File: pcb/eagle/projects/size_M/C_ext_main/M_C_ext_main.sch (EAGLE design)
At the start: 18 parts

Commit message: PCB M.1
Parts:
- removed H.C1, H.C5, H.C6, H.C7, H.C8, H.C9: 100n, rcl:C-EUC0603
- removed H.C3: 1u, rcl:C-EUC0603
- removed H.C4: 10u (22u), rcl:C-EUC0805
- removed H.J1, H.J2: (no value), pinhead2:PINHD-1X6
- removed H.R1, H.R2: 100k, rcl:R-EU_R0603
- removed H.R3: 10k, rcl:R-EU_R0603
- removed H.U1: WT2003S, WT2003S:WT2003S
- removed H.U2: TPA6211, hugo:TPA6211
- removed H.USB: USB-C, hugo:USB-C
- removed JP2: (no value), pinhead2:PINHD-1X4
- added C.C1, C.C2, C.C4: 100n, rcl:C-EUC0603
- added C.C3: 22u, rcl:C-EUC0805
- added C.C5: 10u, rcl:C-EUC0603
- added C.J2: (no value), pinhead2:PINHD-1X6
- added C.R1, C.R2: 2k2, rcl:R-EU_R0603
- added C.R3, C.R4: 0, rcl:R-EU_R0603
- added C.U1: TTGO-MICRO-32, hugo:TTGO-MICRO-32
- added U$1: USB-C, hugo:USB-C
- added U1: CP2104-F03-GM, CP2104:CP2104-F03-GM
- JP1: device pinhead2:PINHD-1X3 -> pinhead2:PINHD-1X4
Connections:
- removed net N$10: H.U1.DM, H.USB.D1_N, H.USB.D2_N
- removed net N$11: H.C3.1, H.U1.VDDLDO, H.USB.VBUS1, H.USB.VBUS2
- removed net N$12: H.C6.1, H.C8.1, H.U1.VOUTR
- removed net N$13: H.C7.1, H.C9.1, H.U1.VOUTL
- removed net N$14: H.R1.2, H.R2.2, H.U2.IN+
- removed net N$15: H.C5.2, H.U2.BYPASS, H.U2.IN-
- removed net N$16: H.U1.SDCLK, JP1.1
- removed net N$17: H.C6.2, H.R1.1
- removed net N$18: H.C7.2, H.R2.1
- removed net N$19: H.U1.SDDAT, JP1.3
- removed net N$3: H.J1.5, H.U2.VO-
- removed net N$4: H.J2.3, H.U1.RX
- removed net N$5: H.J2.4, H.U1.TX
- removed net N$6: H.J1.6, H.U2.VO+
- removed net N$7: H.J1.3, H.R3.1, H.U2.SHTDWN
- removed net N$8: H.U1.SDCMD, JP1.2
- removed net N$9: H.U1.DP, H.USB.D1_P, H.USB.D2_P
- new net PROG: C.R4.1, C.R4.2, C.U1.IO0, U1.!DTR
- new net RESET: C.R3.1, C.R3.2, C.U1.EN, U1.!RTS
- new net RX: C.U1.TXD0, U1.RXD
- new net SCL: C.J2.1, C.R1.1, C.U1.IO22
- new net SDA: C.J2.2, C.R2.1, C.U1.IO21
- new net TX: C.U1.RXD0, U1.TXD
- new net VUSB: C.C4.2, C.C5.2, JP1.1, U$1.VBUS1, U$1.VBUS2, U1.REGIN, U1.VBUS
- net GND: now also C.C1.2, C.C2.2, C.C3.2, C.C4.1, C.C5.1, C.J2.6, C.U1.GND, C.U1.GND2, C.U1.GND3, JP1.4, U$1.GND1, U$1.GND2, U1.GND; no longer H.C1.2, H.C3.2, H.C4.1, H.C5.1, H.J1.4, H.J2.6, H.U1.AVSS, H.U1.DVSS, H.U2.GND, H.USB.GND1, H.USB.GND2, JP2.4
- net N$1: now also U$1.D1_N, U1.DN; no longer H.C8.2, H.J1.2
- net N$2: now also U$1.D1_P, U1.DP; no longer H.C9.2, H.J1.1
- net VCC: now also C.C1.1, C.C2.1, C.C3.1, C.R1.2, C.R2.2, C.U1.3V3, JP1.3, U1.VDD; no longer H.C1.1, H.C4.2, H.R3.2, H.U1.VDDIO, H.U2.VDD, JP2.3

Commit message: updated PCBS after the version 1 delivery
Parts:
- removed C.C4: 100n, rcl:C-EUC0603
- added C.R5: 5K1, rcl:R-EU_R0603
- added C.R6: 5k1, rcl:R-EU_R0603
- C.C5: value 10u -> 1u
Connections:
- new net N$3: C.R6.2, U$1.CC1
- new net N$4: C.R5.2, U$1.CC2
- net GND: now also C.R5.1, C.R6.1; no longer C.C4.1
- net N$1: now also U$1.D2_N
- net N$2: now also U$1.D2_P
- net VCC: now also U1.VIO
- net VUSB: no longer C.C4.2
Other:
- moved on the sheet: U$1

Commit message: updated PCBs for version 2
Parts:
- added C.F1, C.F2: (no value), rcl:R-EU_R0805
- added PROGRAMMING: TPB1,27, testpad:TPB1,27
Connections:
- new net N$5: C.F2.2, JP1.3
- new net N$6: C.F1.2, JP1.1
- new net N$7: PROGRAMMING.TP, U1.!RST!
- net VCC: now also C.F2.1; no longer JP1.3
- net VUSB: now also C.F1.1; no longer JP1.1
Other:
- moved on the sheet: C.C2, C.C5, C.R3, C.R4, C.R5, C.R6, JP1, U$1, U1

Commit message: closed PCB version M.2
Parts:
- renumbered PROGRAMMING to PROG
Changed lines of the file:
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@@
 <part name="C.F2" library="rcl" library_urn="urn:adsk.eagle:library:334" deviceset="R-EU_" device="R0805" package3d_urn="urn:adsk.eagle:package:23553/2"/>
 <part name="C.F1" library="rcl" library_urn="urn:adsk.eagle:library:334" deviceset="R-EU_" device="R0805" package3d_urn="urn:adsk.eagle:package:23553/2"/>
-<part name="PROGRAMMING" library="testpad" library_urn="urn:adsk.eagle:library:385" deviceset="TP" device="B1,27" package3d_urn="urn:adsk.eagle:package:27944/2"/>
+<part name="PROG" library="testpad" library_urn="urn:adsk.eagle:library:385" deviceset="TP" device="B1,27" package3d_urn="urn:adsk.eagle:package:27944/2"/>
 </parts>
 <sheets>
@@
 <attribute name="VALUE" x="168.91" y="65.659" size="1.778" layer="96"/>
 </instance>
-<instance part="PROGRAMMING" gate="G$1" x="119.38" y="157.48" smashed="yes">
+<instance part="PROG" gate="G$1" x="119.38" y="157.48" smashed="yes">
 <attribute name="NAME" x="123.19" y="146.05" size="1.778" layer="95" rot="R90"/>
 <attribute name="TP_SIGNAL_NAME" x="120.65" y="156.21" size="1.778" layer="97"/>
@@
 <pinref part="U1" gate="IC" pin="!RST!"/>
 <wire x1="119.38" y1="154.94" x2="116.84" y2="154.94" width="0.1524" layer="91"/>
-<pinref part="PROGRAMMING" gate="G$1" pin="TP"/>
-</segment>
-</net>
+<pinref part="PROG" gate="G$1" pin="TP"/>
+</segment>
+</net>

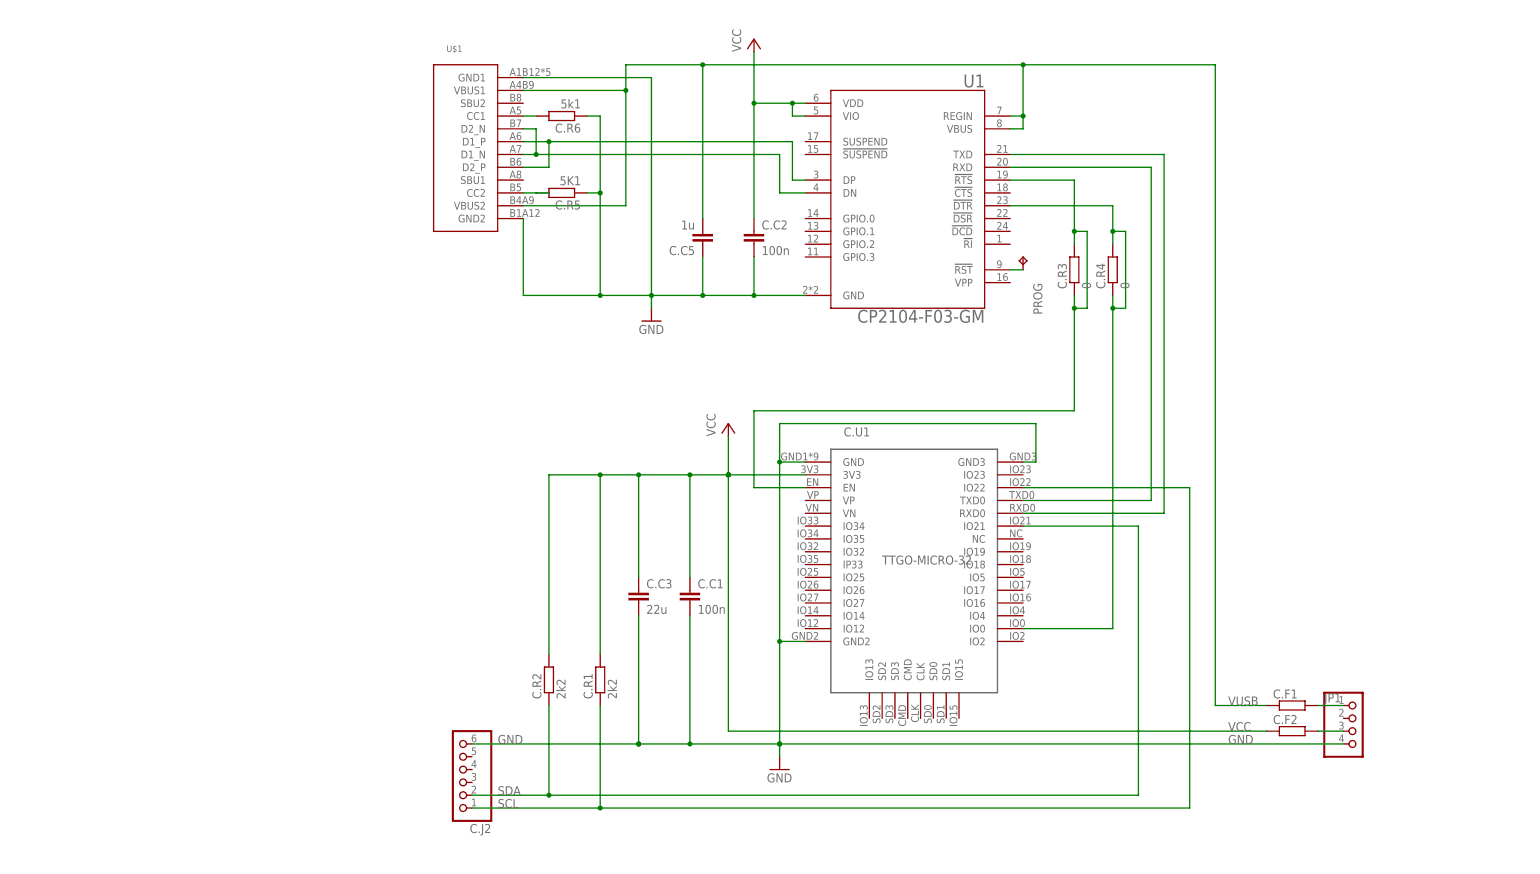
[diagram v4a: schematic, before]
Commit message: updated main board - added 5 to 3.3V regulator becaues one in CP is too weak updated power board - added shotky diode to FET to be sure it works as expected
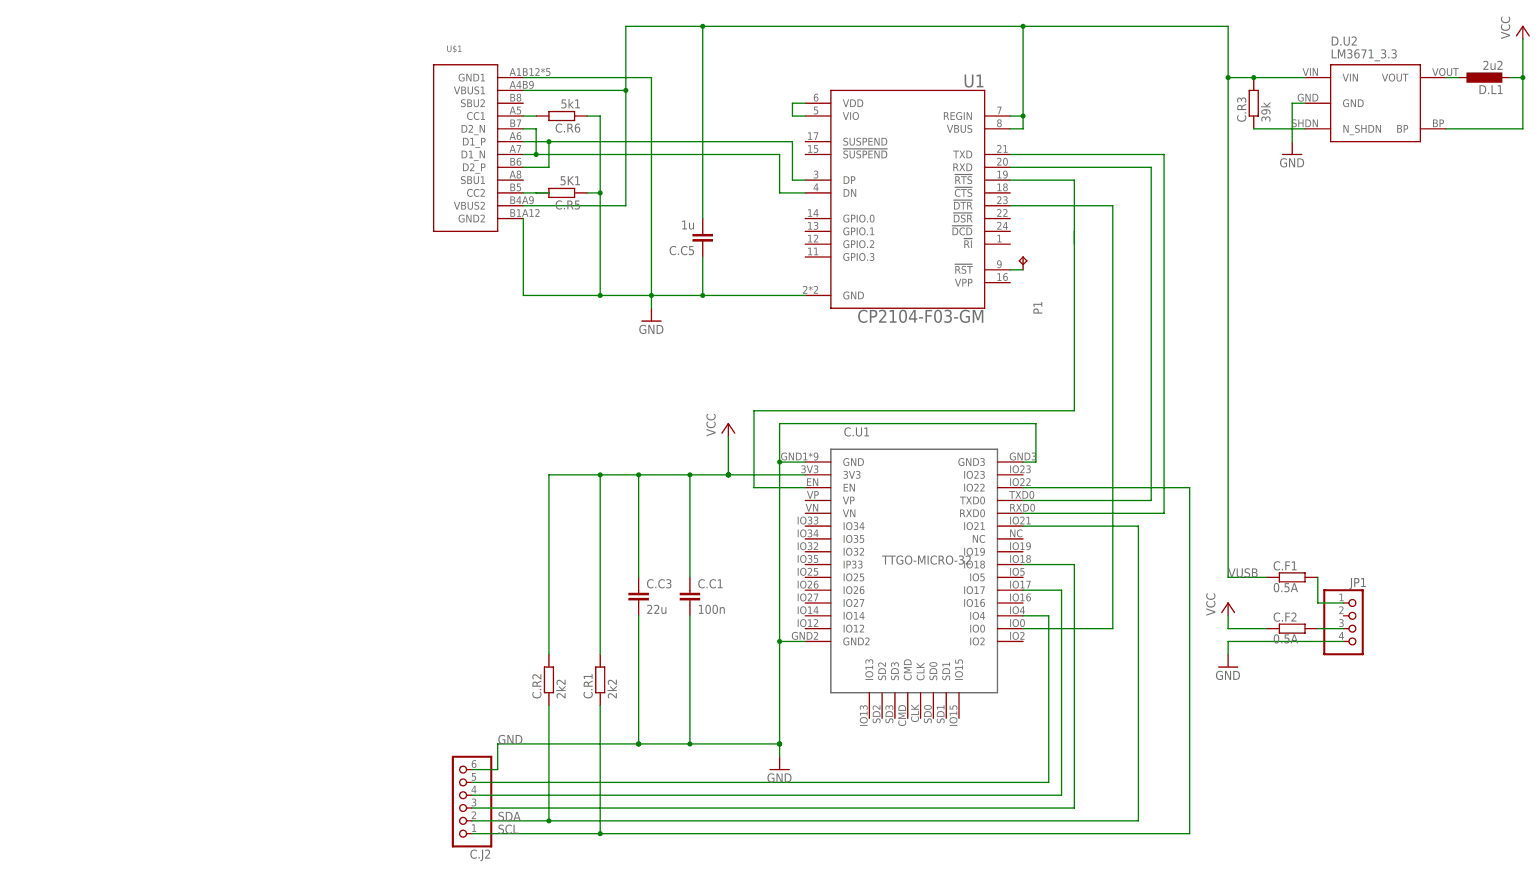
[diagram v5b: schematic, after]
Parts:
- removed C.C2: 100n, rcl:C-EUC0603
- removed C.R4: 0, rcl:R-EU_R0603
- added D.L1: 2u2, rcl:L-EUL3230M
- added D.U2: LM3671_3.3, !stavebnice03:STABILISER_APE8865
- C.F1, C.F2: value (none) -> 0.5A
- C.R3: value 0 -> 39k
- renumbered PROG to P1
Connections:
- new net N$10: D.L1.1, D.U2.VOUT
- new net N$11: C.R3.1, D.U2.N_SHDN
- new net N$12: C.J2.5, C.U1.IO4
- new net N$13: C.J2.4, C.U1.IO17
- new net N$14: C.J2.3, C.U1.IO18
- new net N$8: U1.VDD, U1.VIO
- net GND: now also D.U2.GND; no longer C.C2.2
- net PROG: no longer C.R4.1, C.R4.2
- net RESET: no longer C.R3.1, C.R3.2
- net VCC: now also D.L1.2, D.U2.BP; no longer C.C2.1, U1.VDD, U1.VIO
- net VUSB: now also C.R3.2, D.U2.VIN
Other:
- moved on the sheet: C.F1, C.F2, C.J2, C.R3, JP1

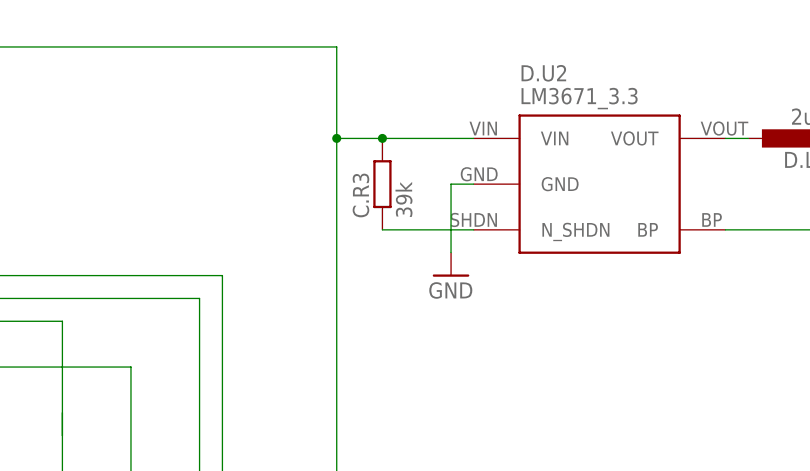
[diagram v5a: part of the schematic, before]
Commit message: main and switch pcbs adjusted
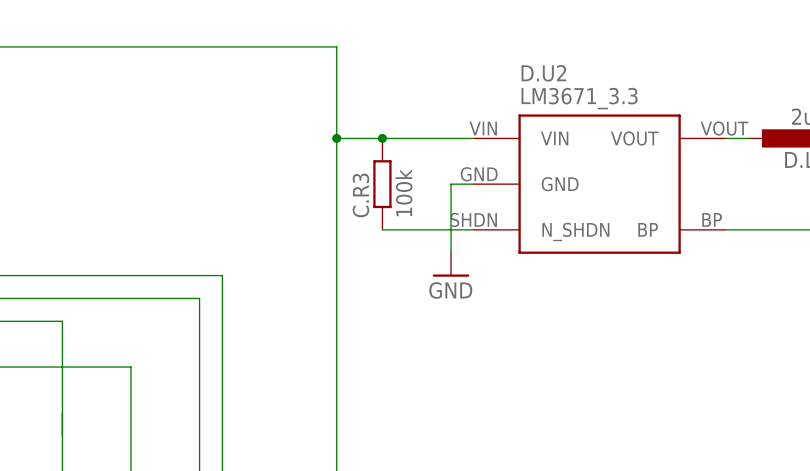
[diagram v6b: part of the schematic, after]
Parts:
- C.R3: value 39k -> 100k
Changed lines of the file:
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@@
 <part name="D.U2" library="!stavebnice03" deviceset="STABILISER_APE8865" device="" value="LM3671_3.3"/>
 <part name="D.L1" library="rcl" library_urn="urn:adsk.eagle:library:334" deviceset="L-EU" device="L3230M" package3d_urn="urn:adsk.eagle:package:23481/3" value="2u2"/>
-<part name="C.R3" library="rcl" library_urn="urn:adsk.eagle:library:334" deviceset="R-EU_" device="R0603" package3d_urn="urn:adsk.eagle:package:23555/3" value="39k"/>
+<part name="C.R3" library="rcl" library_urn="urn:adsk.eagle:library:334" deviceset="R-EU_" device="R0603" package3d_urn="urn:adsk.eagle:package:23555/3" value="100k"/>
 <part name="GND3" library="supply1" library_urn="urn:adsk.eagle:library:371" deviceset="GND" device=""/>
 <part name="P+3" library="supply1" library_urn="urn:adsk.eagle:library:371" deviceset="VCC" device=""/>

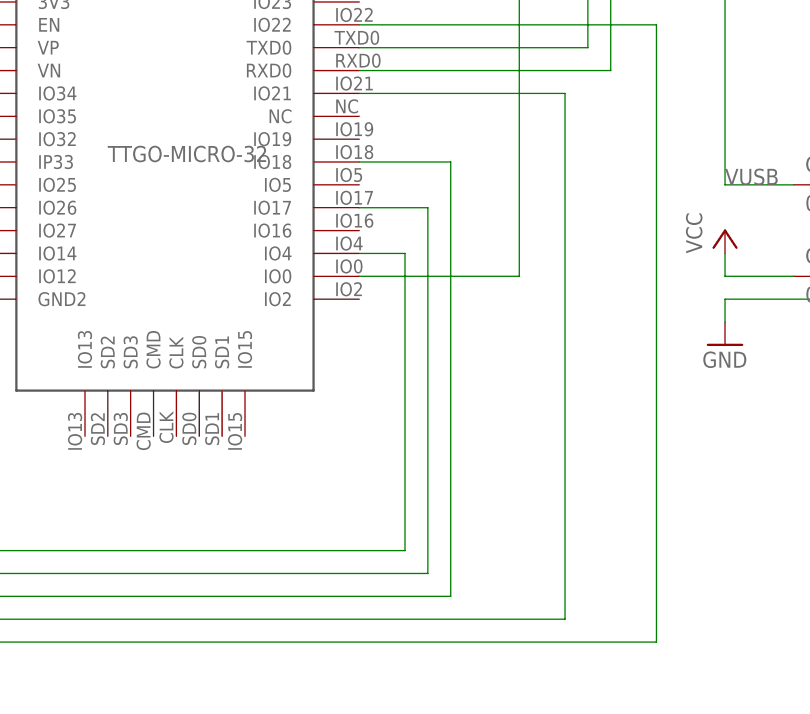
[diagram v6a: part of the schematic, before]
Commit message: changed one data bit to be compatible with T-micro32+
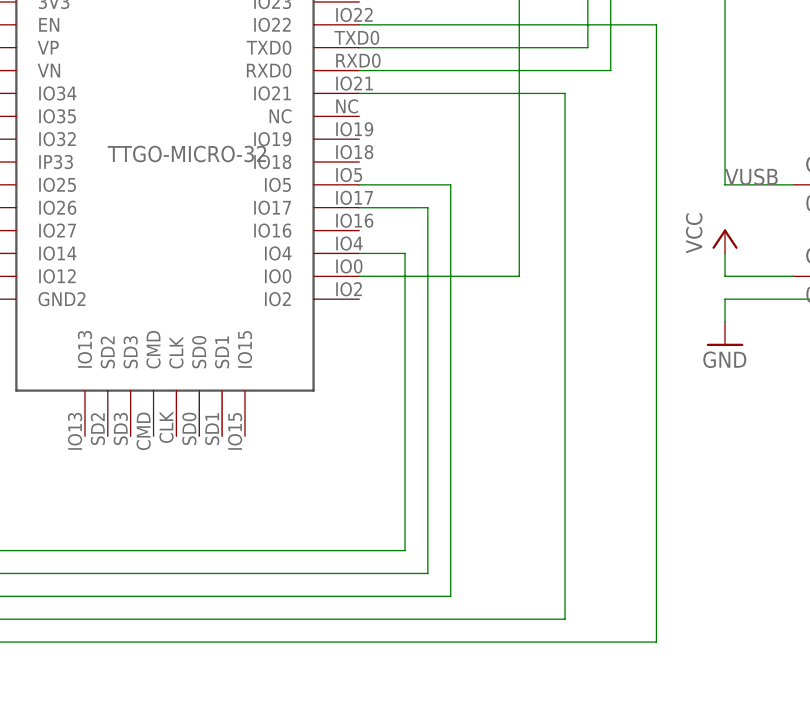
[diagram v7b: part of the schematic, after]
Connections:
- net N$14: now also C.U1.IO5; no longer C.U1.IO18
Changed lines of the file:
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@@
 <net name="N$14" class="0">
 <segment>
-<pinref part="C.U1" gate="G$1" pin="IO18"/>
-<wire x1="119.38" y1="96.52" x2="129.54" y2="96.52" width="0.1524" layer="91"/>
-<wire x1="129.54" y1="96.52" x2="129.54" y2="48.26" width="0.1524" layer="91"/>
 <pinref part="C.J2" gate="A" pin="3"/>
+<wire x1="129.54" y1="93.98" x2="129.54" y2="48.26" width="0.1524" layer="91"/>
 <wire x1="129.54" y1="48.26" x2="10.16" y2="48.26" width="0.1524" layer="91"/>
+<pinref part="C.U1" gate="G$1" pin="IO5"/>
+<wire x1="119.38" y1="93.98" x2="129.54" y2="93.98" width="0.1524" layer="91"/>
 </segment>
 </net>

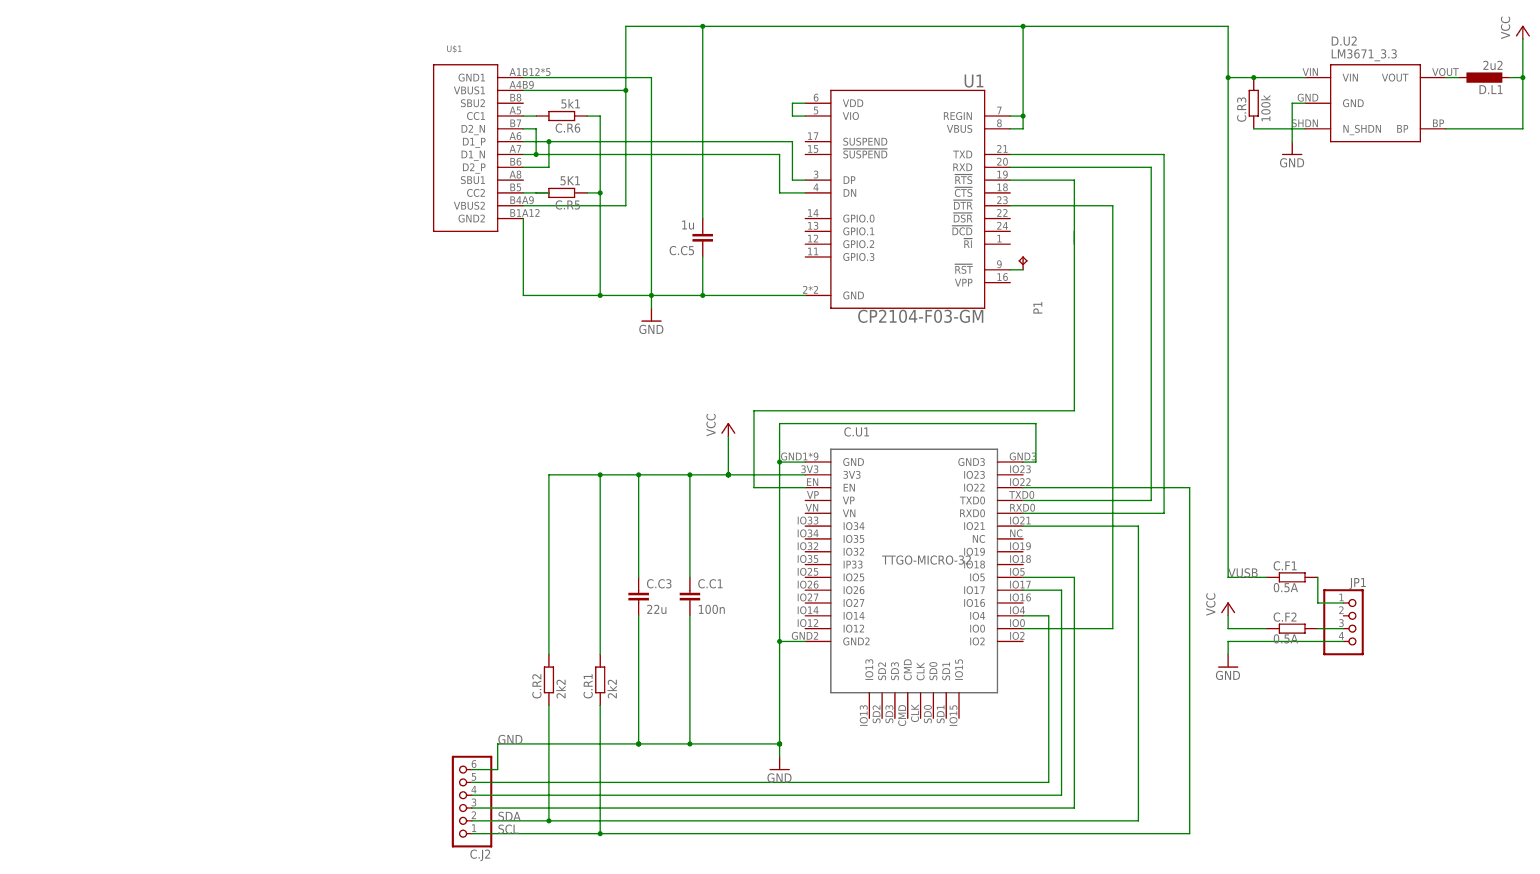
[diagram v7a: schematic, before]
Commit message: changes in values LM3671_3.3 -> MCP1603T-330I
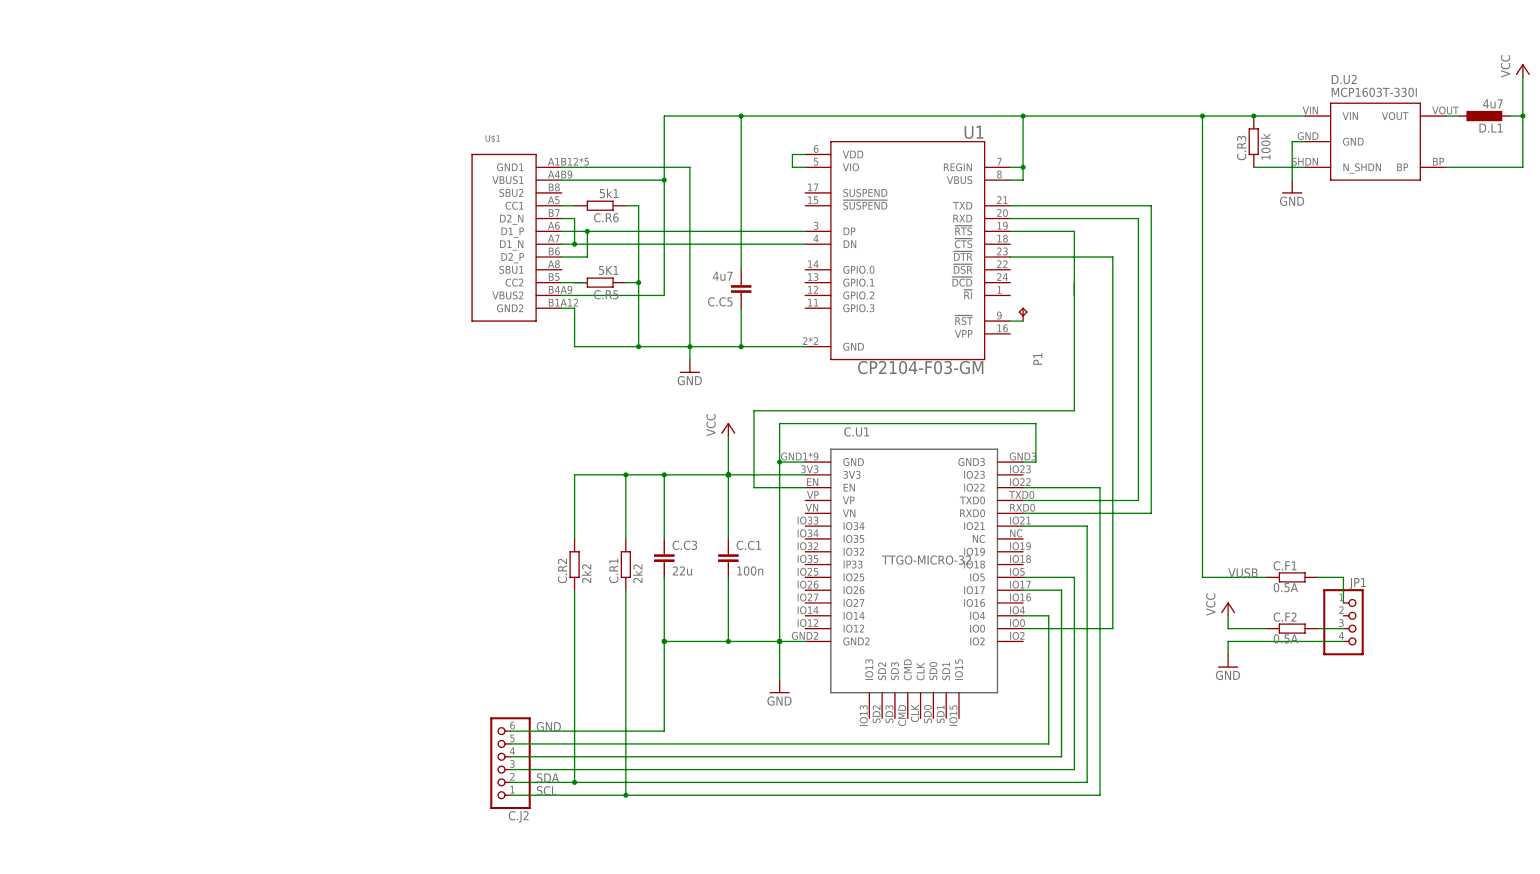
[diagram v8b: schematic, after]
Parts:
- C.C5: value 1u -> 4u7
- D.L1: value 2u2 -> 4u7
- D.U2: value LM3671_3.3 -> MCP1603T-330I
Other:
- moved on the sheet: C.C1, C.C3, C.C5, C.J2, C.R1, C.R2, C.R3, C.R5, C.R6, D.L1, D.U2, P1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
